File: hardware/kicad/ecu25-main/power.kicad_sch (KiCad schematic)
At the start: 27 parts, among them J1 Screw_Terminal_BATT, Q1 SQD50P06-15L, U1 LM5164DDA-Q1, U2 TLV75533 (500mA)

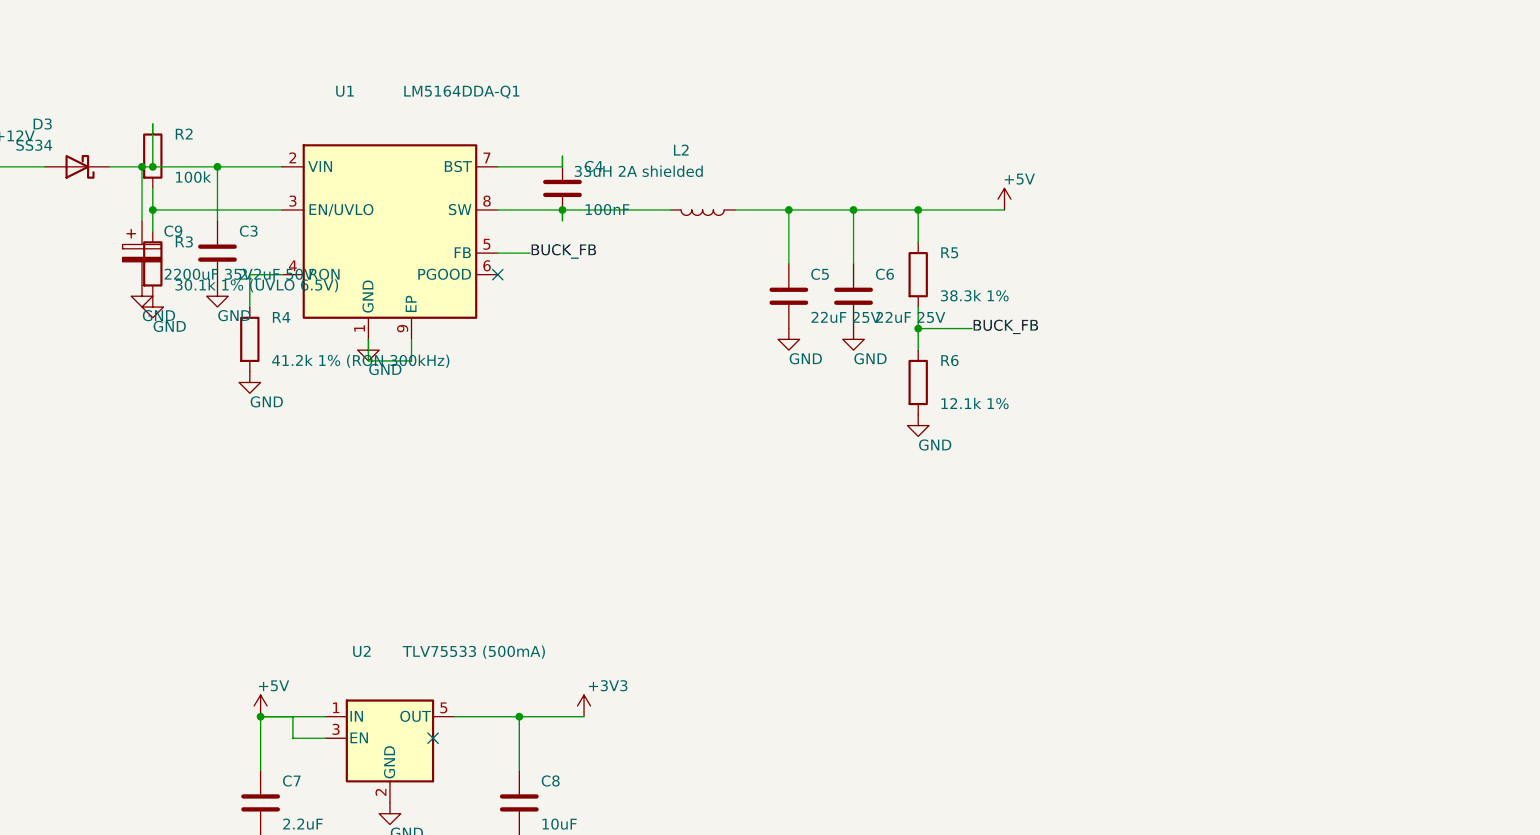
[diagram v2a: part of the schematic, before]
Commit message: Fix SME verification findings; add COT ripple injection and the I/O map
An independent verification pass re-derived the 12 V conversion fixes against
the TI, Omron, Nexperia and ST datasheets instead of trusting the commit
message. The hold-up energy math, the RON/UVLO arithmetic, the modbus_rx
bounds, the AUX refactor and the dry-contact output stage all held. Eleven
majors did not.

Hardware:
- The buck had no ripple-injection network. The LM5164 is constant-on-time:
  it restarts the on-time when FB falls to the 1.2 V reference, so it needs
  >=20 mV of FB ripple IN PHASE with the inductor current. Two 22 uF ceramics
  give 2.7 mV, and that component is capacitive, i.e. out of phase — the
  required series ESR would be 0.287 ohm against the ~2 mohm they actually
  have. The part would have burst-switched: several on-times in close
  succession then a long off-time. Added the datasheet's Type-3 network
  (R7 100k, C10 4.7nF, C11 1nF C0G), which builds the ramp from SW and
  couples it into FB, leaving output ripple untouched. 21 mV at 12.6 V in,
  13 mV at 8 V, against a 12 mV floor
- DIN ground-side pull-up 2.2k -> 1k. 2.2k sat at 2.25 V at 12.6 V but fell
  to 1.59 V during an 8.5 V crank sag — back inside the STM32's indeterminate
  band. The value has to be set by the worst case: V_bat x 1.8/(R+7.4) needs
  R <= 670 ohm to clear V_IH 1.785 V at 8.0 V
- The hold-up node was still the autogenerated Net-(D3-K), so the netclass
  rule and the DRU keyed off a reference designator. Now labelled +12V_HLD
- C9 25 V -> 35 V never reached the orderable BOM: gen_bom.py still said
  "2200 uF 25 V radial" for a node the design puts at 25.6 V
- OUT_COM moved to the Battery class and given a stated ceiling: 4 A total,
  2 A per output, installer fuse 4 A. Four 8 A contacts on a trunk sized for
  4 A needed writing down; it was implied by the netclass and nowhere else
- gen_pcb.py netclass assertion rewritten. It was blind to exactly the
  suffix patterns it was written to pr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
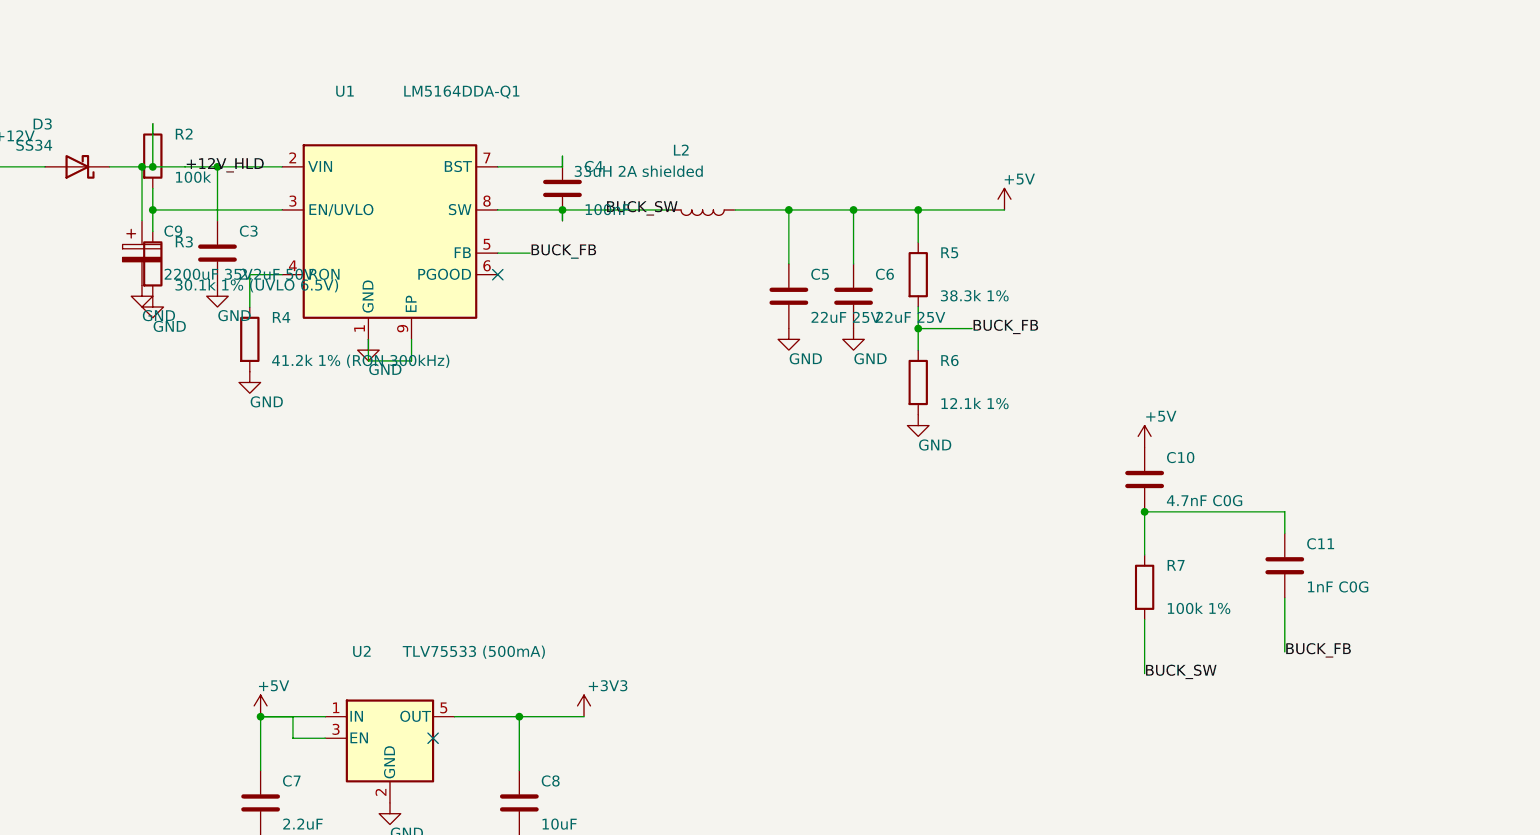
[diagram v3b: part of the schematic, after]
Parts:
- added C10: 4.7nF C0G, Capacitor_SMD:C_0603_1608Metric, symbol Device:C
- added C11: 1nF C0G, Capacitor_SMD:C_0603_1608Metric, symbol Device:C
- added R7: 100k 1%, Resistor_SMD:R_0603_1608Metric, symbol Device:R
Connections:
- net +5V: now also C10.1
- net BUCK_FB: now also C11.2
- net +12V_HLD: now reaches C3.1, C9.1, D3.1 (K), R2.1, U1.2 (VIN)
- net BUCK_SW: now reaches C4.2, L2.2, U1.8 (SW)
- net BUCK_SW: now also R7.2
- new net: C10.2, C11.1, R7.1
